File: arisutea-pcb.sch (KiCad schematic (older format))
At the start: 44 parts, among them J10 PF6, J11 PF7, J12 VCC, J13 D+, J14 D-, J15 GND, J2 MISO, J3 VCC, J4 SCK, J5 MOSI, J6 RES, J7 GND, J8 PF4, J9 PF5, U1 USBLC6-2SC6, U2 ATmega32U4-AU, Y1 Crystal_GND24

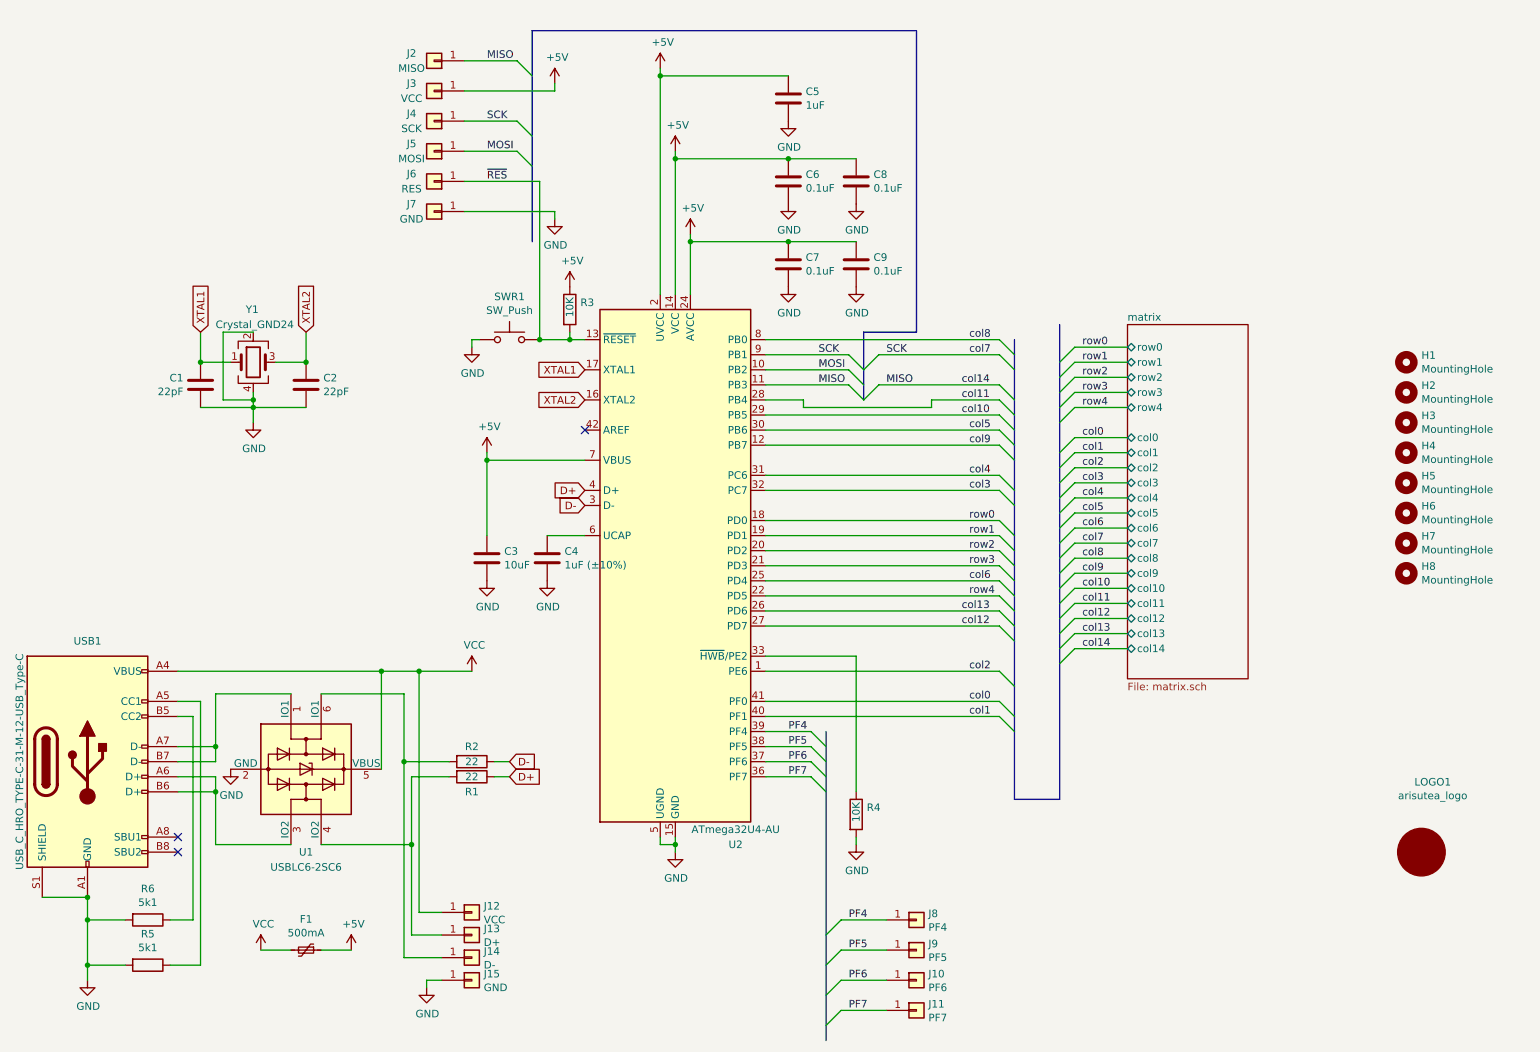
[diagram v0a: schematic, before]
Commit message: routing rework, mounting holes changed, add power LED, crystal adjustment
Moved some routes around...again.  Changed the mounting holes to through holes for plate mounting. Added a power LED, because why not? Adjusted the crystal placement.
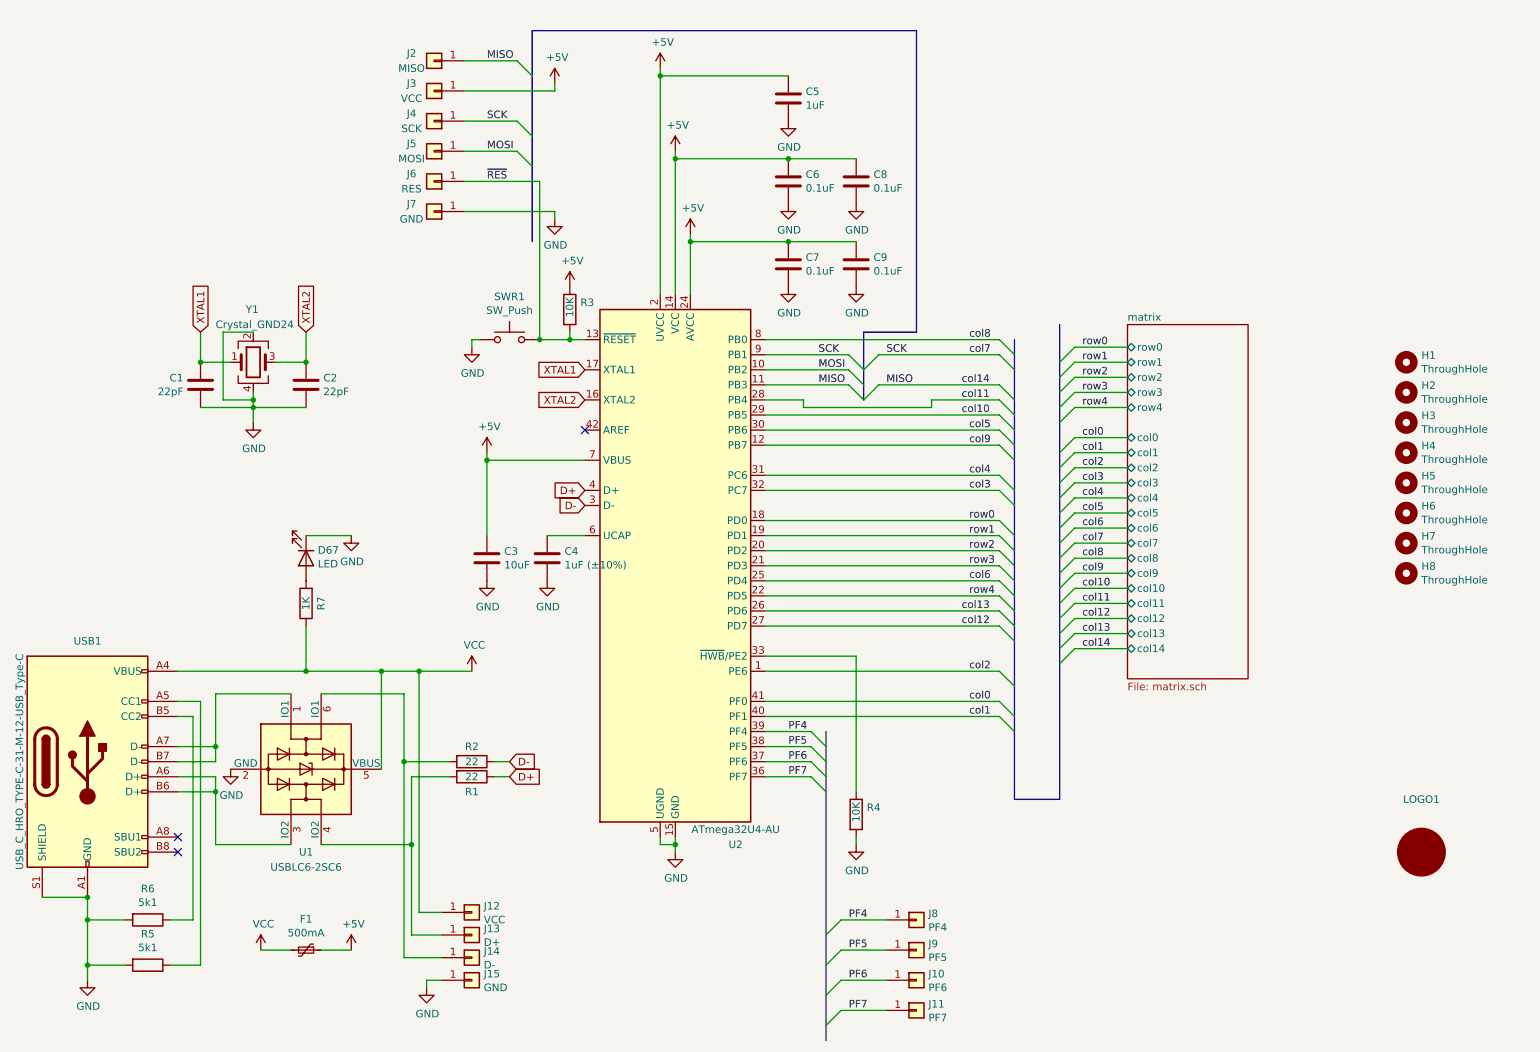
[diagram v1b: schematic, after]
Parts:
- added D67: LED, Diode_SMD:D_SOD-123, symbol Device:LED
- added R7: 1K, Resistor_SMD:R_0805_2012Metric_Pad1.15x1.40mm_HandSolder, symbol Device:R
- H1, H2, H3, H4, H5, H6, H7, H8: value MountingHole -> ThroughHole; footprint MountingHole:MountingHole_2.2mm_M2_Pad -> Mounting_Keyboard_Stabilizer:THROUGH_HOLE_M2
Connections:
- net GND: now also D67.1 (K)
- net VCC: now also R7.1
- new net: D67.2 (A), R7.2
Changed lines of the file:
@@
 EESchema Schematic File Version 4
-LIBS:arisutea-pcb-r1-cache
 EELAYER 30 0
 EELAYER END
@@
 P 9800 2900
 F 0 "H1" H 9900 2946 50  0000 L CNN
-F 1 "MountingHole" H 9900 2855 50  0000 L CNN
-F 2 "MountingHole:MountingHole_2.2mm_M2_Pad" H 9800 2900 50  0001 C CNN
+F 1 "ThroughHole" H 9900 2855 50  0000 L CNN
+F 2 "Mounting_Keyboard_Stabilizer:THROUGH_HOLE_M2" H 9800 2900 50  0001 C CNN
 F 3 "~" H 9800 2900 50  0001 C CNN
 	1    9800 2900
@@
 P 9800 3100
 F 0 "H2" H 9900 3146 50  0000 L CNN
-F 1 "MountingHole" H 9900 3055 50  0000 L CNN
-F 2 "MountingHole:MountingHole_2.2mm_M2_Pad" H 9800 3100 50  0001 C CNN
+F 1 "ThroughHole" H 9900 3055 50  0000 L CNN
+F 2 "Mounting_Keyboard_Stabilizer:THROUGH_HOLE_M2" H 9800 3100 50  0001 C CNN
 F 3 "~" H 9800 3100 50  0001 C CNN
 	1    9800 3100
@@
 P 9800 3300
 F 0 "H3" H 9900 3346 50  0000 L CNN
-F 1 "MountingHole" H 9900 3255 50  0000 L CNN
-F 2 "MountingHole:MountingHole_2.2mm_M2_Pad" H 9800 3300 50  0001 C CNN
+F 1 "ThroughHole" H 9900 3255 50  0000 L CNN
+F 2 "Mounting_Keyboard_Stabilizer:THROUGH_HOLE_M2" H 9800 3300 50  0001 C CNN
 F 3 "~" H 9800 3300 50  0001 C CNN
 	1    9800 3300
@@
 P 9800 3500
 F 0 "H4" H 9900 3546 50  0000 L CNN
-F 1 "MountingHole" H 9900 3455 50  0000 L CNN
-F 2 "MountingHole:MountingHole_2.2mm_M2_Pad" H 9800 3500 50  0001 C CNN
+F 1 "ThroughHole" H 9900 3455 50  0000 L CNN
+F 2 "Mounting_Keyboard_Stabilizer:THROUGH_HOLE_M2" H 9800 3500 50  0001 C CNN
 F 3 "~" H 9800 3500 50  0001 C CNN
 	1    9800 3500
@@
 P 9800 3700
 F 0 "H5" H 9900 3746 50  0000 L CNN
-F 1 "MountingHole" H 9900 3655 50  0000 L CNN
-F 2 "MountingHole:MountingHole_2.2mm_M2_Pad" H 9800 3700 50  0001 C CNN
+F 1 "ThroughHole" H 9900 3655 50  0000 L CNN
+F 2 "Mounting_Keyboard_Stabilizer:THROUGH_HOLE_M2" H 9800 3700 50  0001 C CNN
 F 3 "~" H 9800 3700 50  0001 C CNN
 	1    9800 3700
@@
 P 9800 3900
 F 0 "H6" H 9900 3946 50  0000 L CNN
-F 1 "MountingHole" H 9900 3855 50  0000 L CNN
-F 2 "MountingHole:MountingHole_2.2mm_M2_Pad" H 9800 3900 50  0001 C CNN
+F 1 "ThroughHole" H 9900 3855 50  0000 L CNN
+F 2 "Mounting_Keyboard_Stabilizer:THROUGH_HOLE_M2" H 9800 3900 50  0001 C CNN
 F 3 "~" H 9800 3900 50  0001 C CNN
 	1    9800 3900
@@
 P 9800 4100
 F 0 "H7" H 9900 4146 50  0000 L CNN
-F 1 "MountingHole" H 9900 4055 50  0000 L CNN
-F 2 "MountingHole:MountingHole_2.2mm_M2_Pad" H 9800 4100 50  0001 C CNN
+F 1 "ThroughHole" H 9900 4055 50  0000 L CNN
+F 2 "Mounting_Keyboard_Stabilizer:THROUGH_HOLE_M2" H 9800 4100 50  0001 C CNN
 F 3 "~" H 9800 4100 50  0001 C CNN
 	1    9800 4100
@@
 P 9800 4300
 F 0 "H8" H 9900 4346 50  0000 L CNN
-F 1 "MountingHole" H 9900 4255 50  0000 L CNN
-F 2 "MountingHole:MountingHole_2.2mm_M2_Pad" H 9800 4300 50  0001 C CNN
+F 1 "ThroughHole" H 9900 4255 50  0000 L CNN
+F 2 "Mounting_Keyboard_Stabilizer:THROUGH_HOLE_M2" H 9800 4300 50  0001 C CNN
 F 3 "~" H 9800 4300 50  0001 C CNN
 	1    9800 4300
@@
 	1750 5250 1750 6600
 Wire Wire Line
-	3000 4950 1650 4950
+	3000 4950 2500 4950
 $Comp
 L arisutea-pcb-r1:arisutea_logo LOGO1
 U 1 1 6042E29E
 P 9900 6150
-F 0 "LOGO1" H 9975 6615 50  0000 C CNN
-F 1 "arisutea_logo" H 9975 6524 50  0000 C CNN
+F 0 "LOGO1" H 9900 6500 50  0000 C CNN
+F 1 "arisutea_logo" H 9975 6524 50  0001 C CNN
 F 2 "arisutea:arisutea_logo" H 9900 6500 50  0001 C CNN
 F 3 "" H 9900 6500 50  0001 C CNN
@@
 $EndComp
 Connection ~ 1050 6450
+$Comp
+L Device:LED D67
+U 1 1 6044E1B4
+P 2500 4200
+F 0 "D67" V 2447 4278 50  0000 L CNN
+F 1 "LED" V 2538 4278 50  0000 L CNN
+F 2 "Diode_SMD:D_SOD-123" H 2500 4200 50  0001 C CNN
+F 3 "~" H 2500 4200 50  0001 C CNN
+	1    2500 4200
+	0    1    1    0
+$EndComp
+$Comp
+L Device:R R7
+U 1 1 6045035B
+P 2500 4500
+F 0 "R7" V 2400 4500 50  0000 C CNN
+F 1 "1K" V 2500 4500 50  0000 C CNN
+F 2 "Resistor_SMD:R_0805_2012Metric_Pad1.15x1.40mm_HandSolder" V 2430 4500 50  0001 C CNN
+F 3 "~" H 2500 4500 50  0001 C CNN
+F 4 "C17561" H 2500 4500 50  0001 C CNN "LCSC"
+	1    2500 4500
+	-1   0    0    1
+$EndComp
+Wire Wire Line
+	2500 4650 2500 4950
+Connection ~ 2500 4950
+Wire Wire Line
+	2500 4950 1650 4950
+$Comp
+L power:GND #PWR02
+U 1 1 60459B82
+P 2800 4050
+F 0 "#PWR02" H 2800 3800 50  0001 C CNN
+F 1 "GND" H 2805 3877 50  0000 C CNN
+F 2 "" H 2800 4050 50  0001 C CNN
+F 3 "" H 2800 4050 50  0001 C CNN
+	1    2800 4050
+	1    0    0    -1
+$EndComp
+Wire Wire Line
+	2500 4050 2800 4050
 Wire Bus Line
 	6200 2700 6200 3150

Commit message: house keeping, fixed another silly routing mistake, regen gerbs and BOM
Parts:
- D67: LCSC (none) -> C84259
- R7: footprint Resistor_SMD:R_0805_2012Metric_Pad1.15x1.40mm_HandSolder -> Resistor_SMD:R_0805_2012Metric_Pad1.20x1.40mm_HandSolder; LCSC C17561 -> C17513
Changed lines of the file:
@@
 EESchema Schematic File Version 4
+LIBS:arisutea-pcb-cache
 EELAYER 30 0
 EELAYER END
@@
 Title "Arisutea"
 Date ""
-Rev "1.0"
+Rev "0.3"
 Comp "3x6 Designs"
 Comment1 ""
@@
 F 2 "Diode_SMD:D_SOD-123" H 2500 4200 50  0001 C CNN
 F 3 "~" H 2500 4200 50  0001 C CNN
+F 4 "C84259" V 2500 4200 50  0001 C CNN "LCSC"
 	1    2500 4200
 	0    1    1    0
@@
 F 0 "R7" V 2400 4500 50  0000 C CNN
 F 1 "1K" V 2500 4500 50  0000 C CNN
-F 2 "Resistor_SMD:R_0805_2012Metric_Pad1.15x1.40mm_HandSolder" V 2430 4500 50  0001 C CNN
+F 2 "Resistor_SMD:R_0805_2012Metric_Pad1.20x1.40mm_HandSolder" V 2430 4500 50  0001 C CNN
 F 3 "~" H 2500 4500 50  0001 C CNN
-F 4 "C17561" H 2500 4500 50  0001 C CNN "LCSC"
+F 4 "C17513" H 2500 4500 50  0001 C CNN "LCSC"
 	1    2500 4500
 	-1   0    0    1

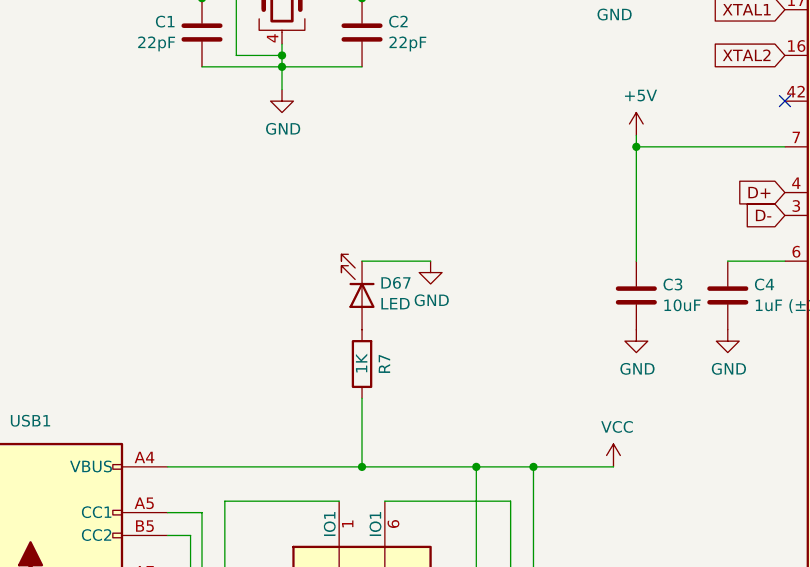
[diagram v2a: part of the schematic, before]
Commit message: footprint and trace cleanup
Changed some footprints to show clearer positioning of U1, U2 and Y1 as well as all the key switch diodes on the silkscreen.

Correct footprint and name for LED.

Moved a couple of traces around slightly for aesthetics.

Removed some trace tails that were just hanging out.
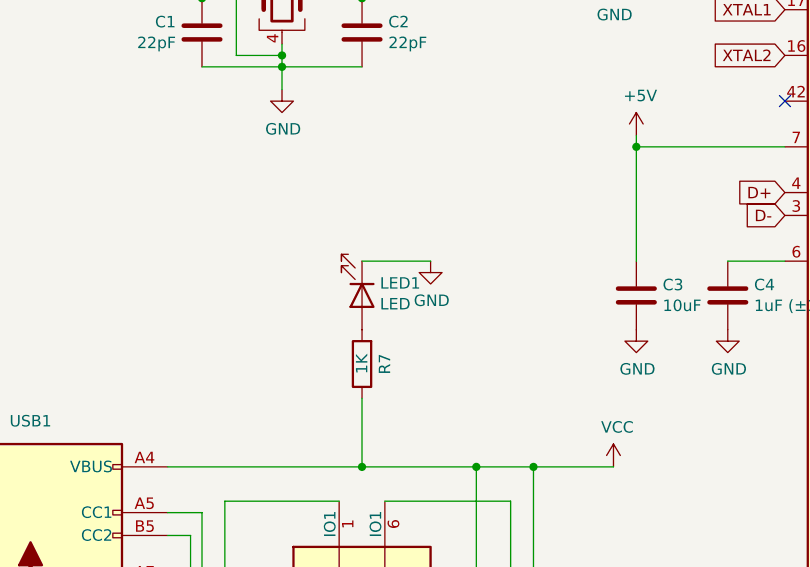
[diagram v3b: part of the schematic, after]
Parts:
- LED1: renamed from D67; footprint Diode_SMD:D_SOD-123 -> LED_SMD:LED_0805_2012Metric_Pad1.15x1.40mm_HandSolder
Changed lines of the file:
@@
 Connection ~ 1050 6450
 $Comp
-L Device:LED D67
+L Device:LED LED1
 U 1 1 6044E1B4
 P 2500 4200
-F 0 "D67" V 2447 4278 50  0000 L CNN
+F 0 "LED1" V 2447 4278 50  0000 L CNN
 F 1 "LED" V 2538 4278 50  0000 L CNN
-F 2 "Diode_SMD:D_SOD-123" H 2500 4200 50  0001 C CNN
+F 2 "LED_SMD:LED_0805_2012Metric_Pad1.15x1.40mm_HandSolder" H 2500 4200 50  0001 C CNN
 F 3 "~" H 2500 4200 50  0001 C CNN
 F 4 "C84259" V 2500 4200 50  0001 C CNN "LCSC"

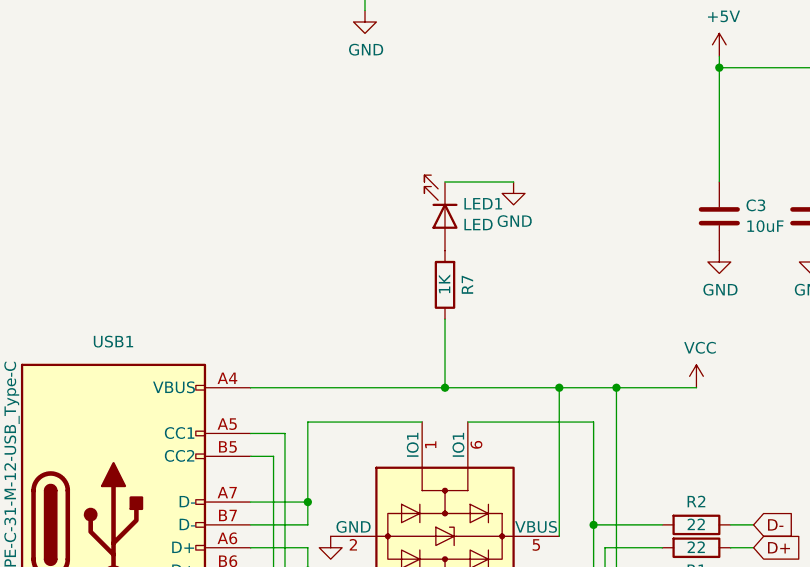
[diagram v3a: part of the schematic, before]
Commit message: versioning to 0.4
remove LED...../sigh
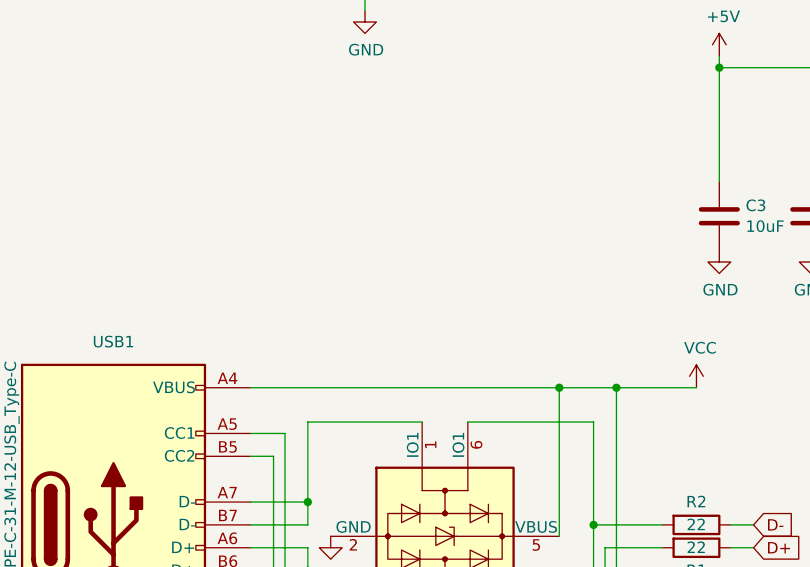
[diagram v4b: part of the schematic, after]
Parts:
- removed LED1: LED, LED_SMD:LED_0805_2012Metric_Pad1.15x1.40mm_HandSolder, symbol Device:LED
- removed R7: 1K, Resistor_SMD:R_0805_2012Metric_Pad1.20x1.40mm_HandSolder, symbol Device:R
- Y1: footprint Crystal:Crystal_SMD_SeikoEpson_FA238-4Pin_3.2x2.5mm_HandSoldering -> Crystal:Crystal_SMD_TXC_7M-4Pin_3.2x2.5mm_HandSoldering
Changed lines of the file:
@@
 Title "Arisutea"
 Date ""
-Rev "0.3"
+Rev "0.4"
 Comp "3x6 Designs"
 Comment1 ""
@@
 Wire Wire Line
 	1750 5250 1750 6600
-Wire Wire Line
-	3000 4950 2500 4950
 $Comp
 L arisutea-pcb-r1:arisutea_logo LOGO1
@@
 F 0 "Y1" H 2100 3250 50  0000 L CNN
 F 1 "Crystal_GND24" H 1900 3150 50  0000 L CNN
-F 2 "Crystal:Crystal_SMD_SeikoEpson_FA238-4Pin_3.2x2.5mm_HandSoldering" H 2150 2900 50  0001 C CNN
+F 2 "Crystal:Crystal_SMD_TXC_7M-4Pin_3.2x2.5mm_HandSoldering" H 2150 2900 50  0001 C CNN
 F 3 "~" H 2150 2900 50  0001 C CNN
 F 4 "C89371" H 2150 2900 50  0001 C CNN "LCSC"
@@
 $EndComp
 Connection ~ 1050 6450
-$Comp
-L Device:LED LED1
-U 1 1 6044E1B4
-P 2500 4200
-F 0 "LED1" V 2447 4278 50  0000 L CNN
-F 1 "LED" V 2538 4278 50  0000 L CNN
-F 2 "LED_SMD:LED_0805_2012Metric_Pad1.15x1.40mm_HandSolder" H 2500 4200 50  0001 C CNN
-F 3 "~" H 2500 4200 50  0001 C CNN
-F 4 "C84259" V 2500 4200 50  0001 C CNN "LCSC"
-	1    2500 4200
-	0    1    1    0
-$EndComp
-$Comp
-L Device:R R7
-U 1 1 6045035B
-P 2500 4500
-F 0 "R7" V 2400 4500 50  0000 C CNN
-F 1 "1K" V 2500 4500 50  0000 C CNN
-F 2 "Resistor_SMD:R_0805_2012Metric_Pad1.20x1.40mm_HandSolder" V 2430 4500 50  0001 C CNN
-F 3 "~" H 2500 4500 50  0001 C CNN
-F 4 "C17513" H 2500 4500 50  0001 C CNN "LCSC"
-	1    2500 4500
-	-1   0    0    1
-$EndComp
-Wire Wire Line
-	2500 4650 2500 4950
-Connection ~ 2500 4950
-Wire Wire Line
-	2500 4950 1650 4950
-$Comp
-L power:GND #PWR02
-U 1 1 60459B82
-P 2800 4050
-F 0 "#PWR02" H 2800 3800 50  0001 C CNN
-F 1 "GND" H 2805 3877 50  0000 C CNN
-F 2 "" H 2800 4050 50  0001 C CNN
-F 3 "" H 2800 4050 50  0001 C CNN
-	1    2800 4050
-	1    0    0    -1
-$EndComp
-Wire Wire Line
-	2500 4050 2800 4050
 Wire Bus Line
 	6200 2700 6200 3150
@@
 Wire Bus Line
 	7200 2750 7200 5800
+Wire Wire Line
+	1650 4950 3000 4950
 $EndSCHEMATC

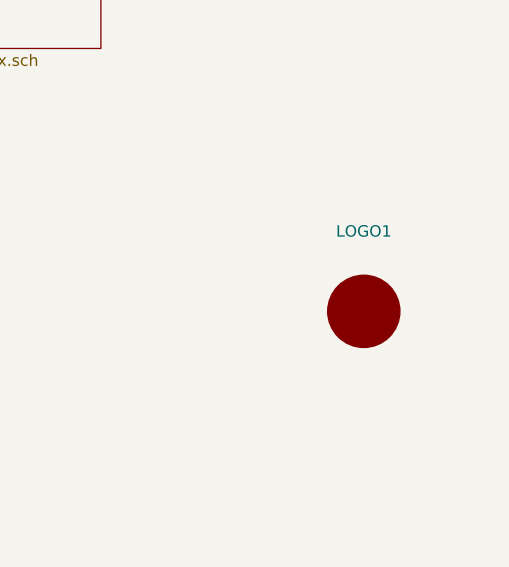
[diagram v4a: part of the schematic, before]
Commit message: library, silkscreen and gerber update
I moved all the footprints into a single library so that if folks don't have the particular lib they won't have to go and search for it or try to replace. Silkscreen was updated again to show clearer positioning of components and gerbers updated to most recent. Version number isn't changing as no big updates were made.
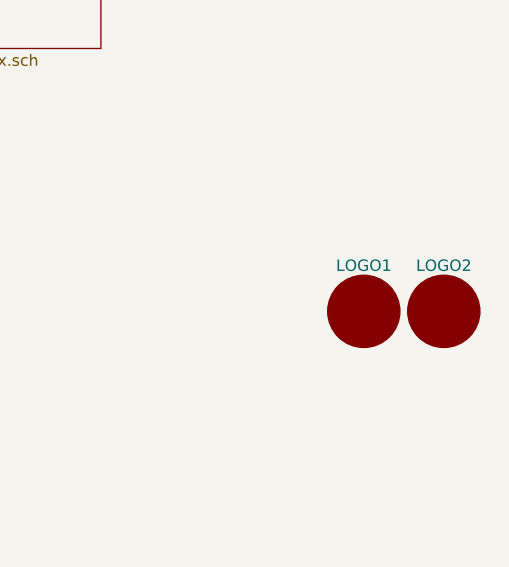
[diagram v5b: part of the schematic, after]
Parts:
- added LOGO2: arisutea_logo, arisutea:arisutea_logo, symbol arisutea-pcb-r1:arisutea_logo
- C1, C2, C3, C4, C5, C6, C7, C8, C9: footprint Capacitor_SMD:C_0805_2012Metric_Pad1.18x1.45mm_HandSolder -> arisutea:C_0805_2012Metric_Pad1.18x1.45mm_HandSolder
- F1: footprint Fuse:Fuse_1206_3216Metric_Pad1.42x1.75mm_HandSolder -> arisutea:Fuse_1206_3216Metric_Pad1.42x1.75mm_HandSolder
- H1, H2, H3, H4, H5, H6, H7, H8: footprint Mounting_Keyboard_Stabilizer:THROUGH_HOLE_M2 -> arisutea:Plated_Through_Hole_M2
- J10, J11, J12, J13, J14, J15, J2, J3, J4, J5, J6, J7, J8, J9: footprint Connector_PinHeader_2.54mm:PinHeader_1x01_P2.54mm_Vertical -> arisutea:PinHeader_1x01_P2.54mm_Vertical
- R1, R2, R3, R4, R5, R6: footprint Resistor_SMD:R_0805_2012Metric_Pad1.20x1.40mm_HandSolder -> arisutea:R_0805_2012Metric_Pad1.20x1.40mm_HandSolder
- SWR1: footprint Button_Switch_SMD:SW_SPST_TL3342 -> arisutea:SW_SPST_TL3342
- U1: footprint Package_TO_SOT_SMD:SOT-23-6_Handsoldering -> arisutea:SOT-23-6_Handsoldering
- U2: footprint Package_QFP:TQFP-44_10x10mm_P0.8mm -> arisutea:TQFP-44_10x10mm_P0.8mm
- USB1: footprint USB_Type-C:USB_C_Receptacle_HRO_TYPE-C-31-M-12-HandSoldering -> arisutea:USB_C_Receptacle_HRO_TYPE-C-31-M-12-HandSoldering
- Y1: footprint Crystal:Crystal_SMD_TXC_7M-4Pin_3.2x2.5mm_HandSoldering -> arisutea:Crystal_SMD_TXC_7M-4Pin_3.2x2.5mm_HandSoldering
